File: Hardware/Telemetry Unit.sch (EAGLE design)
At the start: 12 parts, among them IC1 MEGA128-A, Q1 10MHz, U1 MPL3115A2, X1 SMA-142-0701-801/806

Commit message: First Pass at Compact Layout
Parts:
- removed X1: SMA-142-0701-801/806, con-coax:SMA-142-0701-801/806
- added B1: 9V_CLIP, TrackerPeripherals:9V_CLIP
- added C10, C9: 22u, resistor:C-USC0805
- added C11, C7, C8: 22p, resistor:C-USC0603
- added C5, C6: 2.2u, resistor:C-USC0603
- added D1: (no value), diode:DIODE-DO214AC
- added FIX, PWR: (no value), led:LEDSML0603
- added L1: 1.8n, TrackerPeripherals:L_SMALLL0603
- added L2: 6.8u, TrackerPeripherals:L_SMALLL1210
- added R1, R6: 10k, resistor:R-US_R0603
- added R10: 100k, resistor:R-US_R0603
- added R11, R2: 470, resistor:R-US_R0603
- added R3: 30k, resistor:R-US_R0603
- added R7: 40.2k, resistor:R-US_R0603
- added R8: 59k, resistor:R-US_R0603
- added R9: 13k, resistor:R-US_R0603
- added S1: TACT_SW_4.5MM, TrackerPeripherals:TACT_SW_4.5MM
- added U2: AP65111A, TrackerPeripherals:AP65111A
- C1: value (none) -> 2.2u
- GPS1: value TESO-LIV3F -> M20048-1; device ITCPeripherals:TESO-LIV3F -> TrackerPeripherals:M20048-1
- Q1: device crystal:CRYSTALCTS406 -> crystal:CRYSTALHC49UP
- U1: device ITCPeripherals:MPL3115A2 -> TrackerPeripherals:MPL3115A2
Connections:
- net N$4 renamed XTAL2
- net N$5 renamed XTAL1
- new net !GPS_SLP: GPS1.HW_S, IC1.(XCK1)PD5
- new net !RST: IC1.RESET, R1.2, S1.1@A, XB1.COORD_SEL/AD3/DIO3
- new net FIX: GPS1.FIX, IC1.(IC1)PD4, R2.1
- new net N$10: R8.1, U2.FB
- new net N$12: C11.1, U2.BST
- new net N$14: PWR.A, R11.2
- new net N$3: C7.2, GPS1.ANT_IN
- new net N$4: GPS1.AT2, L1.1
- new net N$5: IC1.PF0(ADC0), R3.2, R6.1
- new net N$6: FIX.A, R2.2
- new net N$7: C11.2, L2.1, U2.SW
- new net N$8: R7.2, R8.2, R9.1
- new net N$9: R10.2, U2.EN
- new net PROG_PWR: D1.A, XB1.RF_TX/AD4/DIO4
- new net RF_SLP: IC1.(T1)PD6, XB1.!DTR!/SLEEP_RQ/DI8
- new net VBAT: B1.+, C10.1, D1.C, R10.1, R3.1, U2.VIN
- net +3V3: now also C5.1, C6.1, C8.1, C9.1, GPS1.BV, L2.2, R1.1, R11.1, R7.1; no longer GPS1.VBAT, GPS1.VCC_IO, GPS1.VCC_RF
- net GND: now also B1.-, C10.2, C5.2, C6.2, C8.2, C9.2, FIX.C, GPS1.GND@1, GPS1.GND@10, GPS1.GND@11, GPS1.GND@12, GPS1.GND@13, GPS1.GND@14, GPS1.GND@2, GPS1.GND@3, GPS1.GND@4, GPS1.GND@5, GPS1.GND@6, GPS1.GND@7, GPS1.GND@8, GPS1.GND@9, L1.2, PWR.C, R6.2, R9.2, S1.0@B, U2.GND; no longer GPS1.GND, GPS1.GND_RF@1, GPS1.GND_RF@2, X1.2
- net N$1: now also C7.1, GPS1.ANT_OUT; no longer GPS1.RF_IN, X1.1
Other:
- note added: "0.25 attenuation with 2.56V ADC reference = 1mV per bit battery monitoring up to 10.24V"
- note added: "E2/E3 NC sets 9600 baud rate"

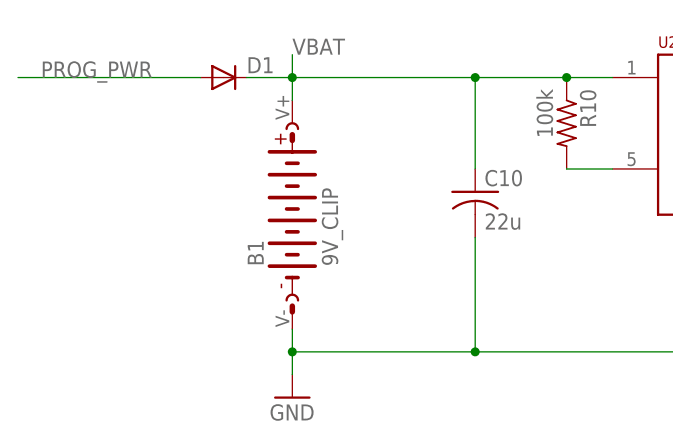
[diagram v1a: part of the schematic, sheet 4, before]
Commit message: Switch to screw terminals for battery
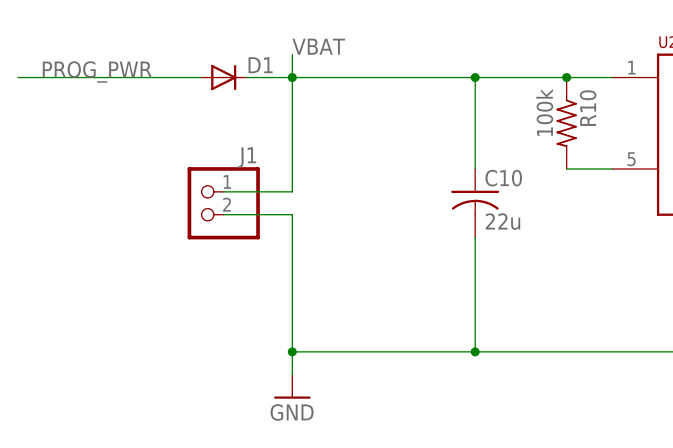
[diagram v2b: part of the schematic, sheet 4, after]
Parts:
- removed B1: 9V_CLIP, TrackerPeripherals:9V_CLIP
- added J1: (no value), TrackerPeripherals:ST_2X1
- C3, C4: value (none) -> 22p
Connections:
- new net N$11: IC1.RESET, S1.1@A
- net !RST: now also S1.1@B; no longer IC1.RESET, S1.1@A
- net GND: now also J1.2; no longer B1.-
- net VBAT: now also J1.1; no longer B1.+

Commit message: Add accelerometer
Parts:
- added C12: 100n, resistor:C-USC0603
- added C13: 2.2u, resistor:C-USC0603
- added U3: LSM6DS3, TrackerPeripherals:LSM6DS3
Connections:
- new net ACCEL_INT: IC1.(OC3B/INT4)PE4, U3.INT1
- net +3V3: now also C12.1, C13.1, U3.VDD, U3.VDDIO
- net GND: now also C12.2, C13.2, U3.GND@1, U3.GND@2
- net SCL: now also U3.SCL
- net SDA: now also U3.SDA

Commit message: Preliminary Signal Routing
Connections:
- removed net N$11: IC1.RESET, S1.1@A
- new net RST2: R1.2, S1.1@B
- net !RST: now also IC1.RESET, S1.1@A; no longer R1.2, S1.1@B
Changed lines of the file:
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@@
-</segment>
-</net>
-<net name="!RST" class="0">
-<segment>
-<label x="15.24" y="116.84" size="1.778" layer="95"/>
-<pinref part="S1" gate="G$1" pin="1@B"/>
-<pinref part="R1" gate="G$1" pin="2"/>
-<wire x1="22.86" y1="119.38" x2="22.86" y2="116.84" width="0.1524" layer="91"/>
-<wire x1="22.86" y1="116.84" x2="15.24" y2="114.3" width="0.1524" layer="91"/>
 </segment>
 </net>
@@
 </segment>
 </net>
-<net name="N$11" class="0">
+<net name="!RST" class="0">
 <segment>
 <pinref part="IC1" gate="G$1" pin="RESET"/>
@@
 <wire x1="15.24" y1="116.84" x2="22.86" y2="114.3" width="0.1524" layer="91"/>
 <wire x1="22.86" y1="114.3" x2="25.4" y2="114.3" width="0.1524" layer="91"/>
+<label x="15.24" y="116.84" size="1.778" layer="95"/>
 </segment>
 </net>
@@
 </segment>
 </net>
+<net name="RST2" class="0">
+<segment>
+<pinref part="S1" gate="G$1" pin="1@B"/>
+<pinref part="R1" gate="G$1" pin="2"/>
+<wire x1="22.86" y1="119.38" x2="22.86" y2="116.84" width="0.1524" layer="91"/>
+<wire x1="22.86" y1="116.84" x2="15.24" y2="114.3" width="0.1524" layer="91"/>
+</segment>
+</net>

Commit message: Merging changes into schematics.
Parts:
- added C14: 100nF, rcl:C-EUC0603
- added IC2: FT232RL, ftdichip:FT232RL
- added J2: 503182-1852, 503182-1852_SD:503182-1852
- added J3: 10118193-0001LF, 10118193-0001LF_microUSB:10118193-0001LF
- added LED1, LED2: (no value), led:LEDCHIP-LED0603
- added R12, R13: 1k, rcl:R-US_R0603
- added R14: 10k, rcl:R-US_R0603
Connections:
- new net CS_SD: IC1.(OC0)PB4, J2.DATA2, R14.1
- new net N$11: IC2.USBDM, J3.D-
- new net N$13: IC2.USBDP, J3.D+
- new net N$15: LED1.C, R12.1
- new net N$16: C14.1, IC2.!DTR
- new net N$17: LED2.C, R13.1
- new net N$18: IC2.CBUS1, R12.2
- new net N$19: IC2.CBUS0, R13.2
- new net V_USB: J3.VUSB
- net !RST: now also C14.2
- net +3V3: now also J2.VDD, R14.2
- net GND: now also IC2.!RESET, IC2.GND, IC2.GND@1, IC2.GND@2, IC2.GND@A, IC2.TEST, J2.SHIELD, J2.VSS, J3.GND, J3.SHIELD
- net MISO: now also J2.DAT0
- net MOSI: now also J2.CMD
- net RX0: now also IC2.TXD
- net SCK: now also J2.CLK
- net TX0: now also IC2.RXD
- net VCC: now also IC2.VCC, IC2.VCCIO, LED1.A, LED2.A

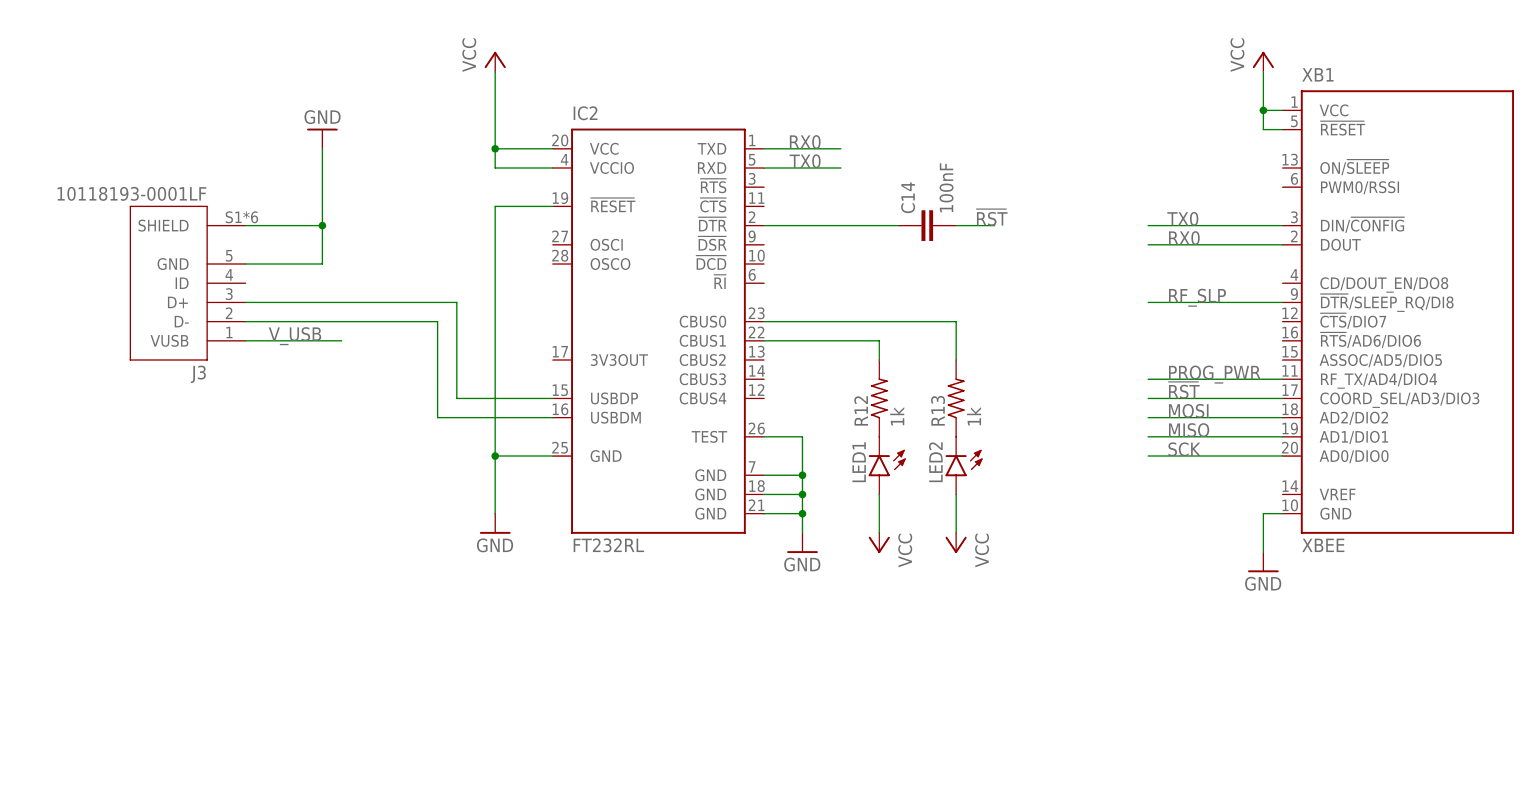
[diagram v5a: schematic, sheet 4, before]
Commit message: Finished merge, updated layout, added ICSP
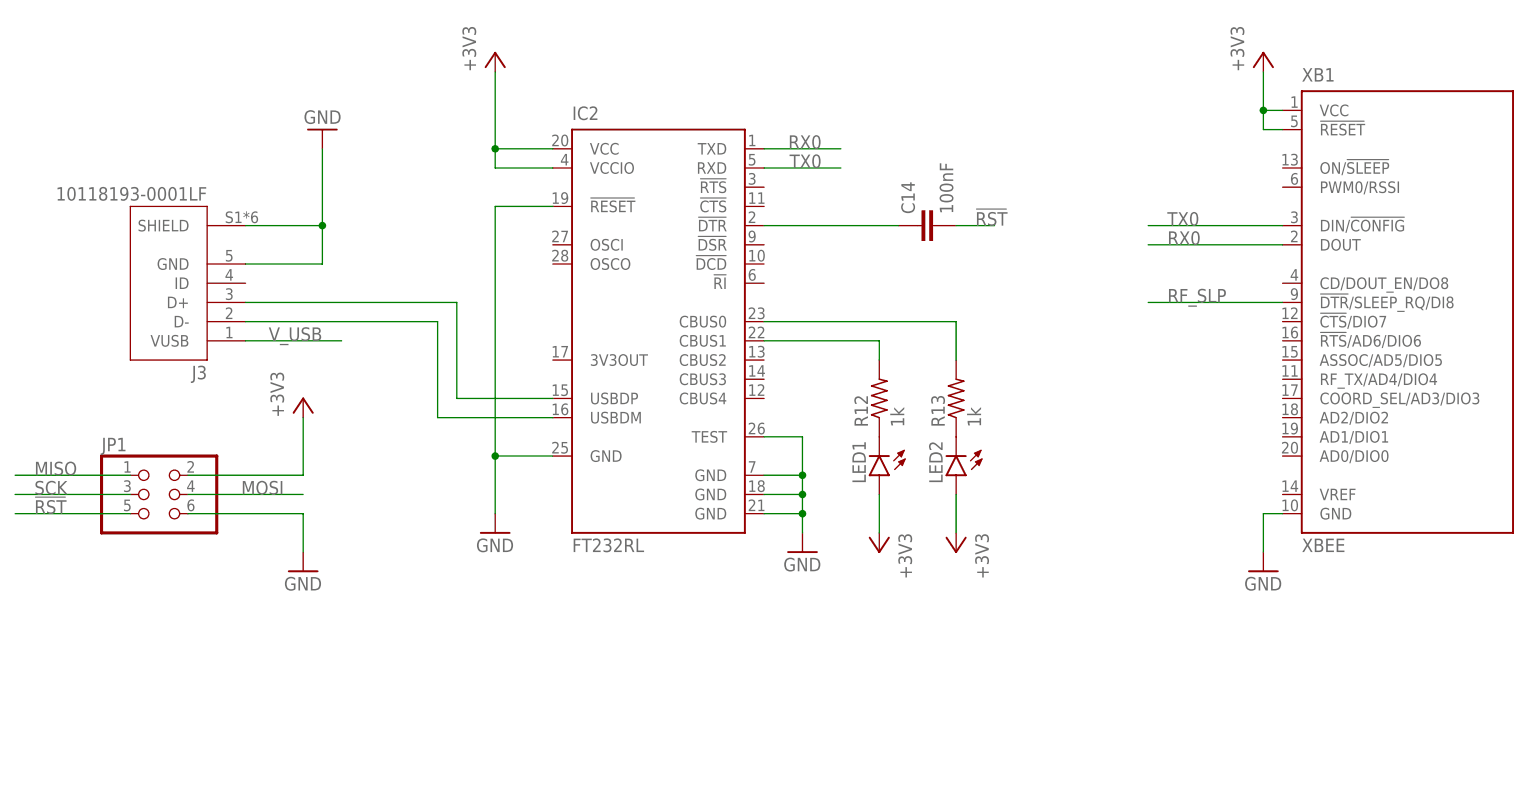
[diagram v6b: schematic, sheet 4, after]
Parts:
- added JP1: (no value), pinhead:PINHD-2X3
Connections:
- removed net PROG_PWR: D1.A, XB1.RF_TX/AD4/DIO4
- removed net VCC: IC2.VCC, IC2.VCCIO, LED1.A, LED2.A, XB1.!RESET, XB1.VCC
- net !RST: now also JP1.5; no longer XB1.COORD_SEL/AD3/DIO3
- net +3V3: now also IC2.VCC, IC2.VCCIO, JP1.2, LED1.A, LED2.A, XB1.!RESET, XB1.VCC
- net GND: now also JP1.6
- net MISO: now also JP1.1; no longer XB1.AD1/DIO1
- net MOSI: now also JP1.4; no longer XB1.AD2/DIO2
- net SCK: now also JP1.3; no longer XB1.AD0/DIO0
- net V_USB: now also D1.A

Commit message: Full Routing Complete?
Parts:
- added C15: 2.2u, resistor:C-USC0603
- added R15, R16: 10k, resistor:R-US_R0603
- renumbered LED1 to RX, LED2 to TX
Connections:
- new net N$20: IC2.TXD, R15.1
- new net N$21: IC2.RXD, R16.1
- net !RST: no longer C14.2, JP1.5
- net +3V3: now also C15.1
- net GND: now also C15.2, GPS1.AT1, S1.0@A
- net RST2: now also C14.2, JP1.5
- net RX0: now also R15.2; no longer IC2.TXD
- net TX0: now also R16.2; no longer IC2.RXD
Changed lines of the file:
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@@
 <part name="R12" library="rcl" library_urn="urn:adsk.eagle:library:334" deviceset="R-US_" device="R0603" package3d_urn="urn:adsk.eagle:package:23555/2" value="1k"/>
 <part name="R13" library="rcl" library_urn="urn:adsk.eagle:library:334" deviceset="R-US_" device="R0603" package3d_urn="urn:adsk.eagle:package:23555/2" value="1k"/>
-<part name="LED1" library="led" library_urn="urn:adsk.eagle:library:259" deviceset="LED" device="CHIP-LED0603" package3d_urn="urn:adsk.eagle:package:15819/3"/>
-<part name="LED2" library="led" library_urn="urn:adsk.eagle:library:259" deviceset="LED" device="CHIP-LED0603" package3d_urn="urn:adsk.eagle:package:15819/3"/>
+<part name="RX" library="led" library_urn="urn:adsk.eagle:library:259" deviceset="LED" device="CHIP-LED0603" package3d_urn="urn:adsk.eagle:package:15819/3"/>
+<part name="TX" library="led" library_urn="urn:adsk.eagle:library:259" deviceset="LED" device="CHIP-LED0603" package3d_urn="urn:adsk.eagle:package:15819/3"/>
 <part name="P+3" library="supply1" library_urn="urn:adsk.eagle:library:371" deviceset="+3V3" device=""/>
 <part name="P+4" library="supply1" library_urn="urn:adsk.eagle:library:371" deviceset="+3V3" device=""/>
@@
 <part name="GND19" library="supply1" library_urn="urn:adsk.eagle:library:371" deviceset="GND" device=""/>
 <part name="P+5" library="supply1" library_urn="urn:adsk.eagle:library:371" deviceset="+3V3" device=""/>
+<part name="C15" library="resistor" library_urn="urn:adsk.eagle:library:348" deviceset="C-US" device="C0603" package3d_urn="urn:adsk.eagle:package:23616/2" value="2.2u"/>
+<part name="R15" library="resistor" library_urn="urn:adsk.eagle:library:348" deviceset="R-US_" device="R0603" package3d_urn="urn:adsk.eagle:package:23555/3" value="10k"/>
+<part name="R16" library="resistor" library_urn="urn:adsk.eagle:library:348" deviceset="R-US_" device="R0603" package3d_urn="urn:adsk.eagle:package:23555/3" value="10k"/>
 </parts>
 <sheets>
@@
 <pinref part="GND7" gate="1" pin="GND"/>
 <pinref part="S1" gate="G$1" pin="0@B"/>
+<pinref part="S1" gate="G$1" pin="0@A"/>
+<wire x1="2.54" y1="116.84" x2="-2.54" y2="116.84" width="0.1524" layer="91"/>
+<wire x1="-2.54" y1="116.84" x2="-2.54" y2="114.3" width="0.1524" layer="91"/>
+<junction x="-2.54" y="114.3"/>
 </segment>
 <segment>
@@
 <pinref part="GND1" gate="1" pin="GND"/>
 <wire x1="73.66" y1="50.8" x2="73.66" y2="48.26" width="0.1524" layer="91"/>
+<pinref part="GPS1" gate="G$1" pin="AT1"/>
+<wire x1="45.72" y1="53.34" x2="45.72" y2="55.88" width="0.1524" layer="91"/>
+<wire x1="45.72" y1="55.88" x2="73.66" y2="55.88" width="0.1524" layer="91"/>
+<wire x1="73.66" y1="55.88" x2="73.66" y2="50.8" width="0.1524" layer="91"/>
+<junction x="73.66" y="50.8"/>
 </segment>
 <segment>
@@
 </instance>
 <instance part="C14" gate="G$1" x="25.4" y="66.04" smashed="yes" rot="R90">
-<attribute name="NAME" x="25.019" y="67.564" size="1.778" layer="95" rot="R90"/>
-<attribute name="VALUE" x="30.099" y="67.564" size="1.778" layer="96" rot="R90"/>
+<attribute name="NAME" x="23.876" y="65.659" size="1.778" layer="95" rot="R180"/>
+<attribute name="VALUE" x="26.416" y="63.119" size="1.778" layer="96" rot="R180"/>
 </instance>
 <instance part="R12" gate="G$1" x="20.32" y="43.18" smashed="yes" rot="R90">
@@
 <attribute name="VALUE" x="33.782" y="39.37" size="1.778" layer="96" rot="R90"/>
 </instance>
-<instance part="LED1" gate="G$1" x="20.32" y="33.02" smashed="yes" rot="R180">
+<instance part="RX" gate="G$1" x="20.32" y="33.02" smashed="yes" rot="R180">
 <attribute name="NAME" x="16.764" y="37.592" size="1.778" layer="95" rot="R270"/>
 <attribute name="VALUE" x="14.605" y="37.592" size="1.778" layer="96" rot="R270"/>
 </instance>
-<instance part="LED2" gate="G$1" x="30.48" y="33.02" smashed="yes" rot="R180">
+<instance part="TX" gate="G$1" x="30.48" y="33.02" smashed="yes" rot="R180">
 <attribute name="NAME" x="26.924" y="37.592" size="1.778" layer="95" rot="R270"/>
 <attribute name="VALUE" x="24.765" y="37.592" size="1.778" layer="96" rot="R270"/>
@@
 <instance part="P+5" gate="G$1" x="-55.88" y="43.18" smashed="yes">
 <attribute name="VALUE" x="-58.42" y="40.64" size="1.778" layer="96" rot="R90"/>
+</instance>
+<instance part="C15" gate="G$1" x="-35.56" y="71.12" smashed="yes">
+<attribute name="NAME" x="-34.544" y="71.755" size="1.778" layer="95"/>
+<attribute name="VALUE" x="-34.544" y="66.929" size="1.778" layer="96"/>
+</instance>
+<instance part="R15" gate="G$1" x="20.32" y="76.2" smashed="yes">
+<attribute name="NAME" x="16.51" y="77.6986" size="1.778" layer="95"/>
+<attribute name="VALUE" x="21.59" y="77.978" size="1.778" layer="96"/>
+</instance>
+<instance part="R16" gate="G$1" x="20.32" y="73.66" smashed="yes">
+<attribute name="NAME" x="16.51" y="70.0786" size="1.778" layer="95"/>
+<attribute name="VALUE" x="21.59" y="70.358" size="1.778" layer="96"/>
 </instance>
 </instances>
@@
 <pinref part="IC2" gate="1" pin="!RESET"/>
 <wire x1="-22.86" y1="68.58" x2="-30.48" y2="68.58" width="0.1524" layer="91"/>
-<wire x1="-30.48" y1="68.58" x2="-30.48" y2="35.56" width="0.1524" layer="91"/>
+<wire x1="-30.48" y1="68.58" x2="-30.48" y2="66.04" width="0.1524" layer="91"/>
 <pinref part="GND17" gate="1" pin="GND"/>
 <pinref part="IC2" gate="1" pin="GND@A"/>
+<wire x1="-30.48" y1="66.04" x2="-30.48" y2="35.56" width="0.1524" layer="91"/>
 <wire x1="-30.48" y1="35.56" x2="-30.48" y2="27.94" width="0.1524" layer="91"/>
 <wire x1="-22.86" y1="35.56" x2="-30.48" y2="35.56" width="0.1524" layer="91"/>
 <junction x="-30.48" y="35.56"/>
+<pinref part="C15" gate="G$1" pin="2"/>
+<wire x1="-35.56" y1="66.04" x2="-30.48" y2="66.04" width="0.1524" layer="91"/>
+<junction x="-30.48" y="66.04"/>
 </segment>
 <segment>
@@
 </segment>
 <segment>
-<pinref part="IC2" gate="1" pin="RXD"/>
-<wire x1="5.08" y1="73.66" x2="15.24" y2="73.66" width="0.1524" layer="91"/>
-<label x="12.7" y="73.66" size="1.778" layer="95" align="bottom-right"/>
+<pinref part="R16" gate="G$1" pin="2"/>
+<wire x1="25.4" y1="73.66" x2="35.56" y2="73.66" width="0.1524" layer="91"/>
+<label x="33.02" y="73.66" size="1.778" layer="95" align="bottom-right"/>
 </segment>
 </net>
@@
 </segment>
 <segment>
-<pinref part="IC2" gate="1" pin="TXD"/>
-<wire x1="5.08" y1="76.2" x2="15.24" y2="76.2" width="0.1524" layer="91"/>
-<label x="12.7" y="76.2" size="1.778" layer="95" align="bottom-right"/>
-</segment>
-</net>
-<net name="!RST" class="0">
-<segment>
-<pinref part="C14" gate="G$1" pin="2"/>
-<wire x1="30.48" y1="66.04" x2="35.56" y2="66.04" width="0.1524" layer="91"/>
-<label x="33.02" y="66.04" size="1.778" layer="95"/>
-</segment>
-<segment>
-<pinref part="JP1" gate="A" pin="5"/>
-<wire x1="-78.74" y1="27.94" x2="-93.98" y2="27.94" width="0.1524" layer="91"/>
-<label x="-91.44" y="27.94" size="1.778" layer="95"/>
+<pinref part="R15" gate="G$1" pin="2"/>
+<wire x1="25.4" y1="76.2" x2="35.56" y2="76.2" width="0.1524" layer="91"/>
+<label x="33.02" y="76.2" size="1.778" layer="95" align="bottom-right"/>
 </segment>
 </net>
@@
 <segment>
 <pinref part="R12" gate="G$1" pin="1"/>
-<pinref part="LED1" gate="G$1" pin="C"/>
+<pinref part="RX" gate="G$1" pin="C"/>
 </segment>
 </net>
@@
 <segment>
 <pinref part="R13" gate="G$1" pin="1"/>
-<pinref part="LED2" gate="G$1" pin="C"/>
+<pinref part="TX" gate="G$1" pin="C"/>
 </segment>
 </net>
@@
 <wire x1="-30.48" y1="73.66" x2="-30.48" y2="76.2" width="0.1524" layer="91"/>
 <junction x="-30.48" y="76.2"/>
+<pinref part="C15" gate="G$1" pin="1"/>
+<wire x1="-35.56" y1="73.66" x2="-30.48" y2="73.66" width="0.1524" layer="91"/>
+<junction x="-30.48" y="73.66"/>
 </segment>
 <segment>
 <pinref part="P+3" gate="G$1" pin="+3V3"/>
-<pinref part="LED1" gate="G$1" pin="A"/>
+<pinref part="RX" gate="G$1" pin="A"/>
 <wire x1="20.32" y1="25.4" x2="20.32" y2="30.48" width="0.1524" layer="91"/>
 </segment>
 <segment>
 <pinref part="P+4" gate="G$1" pin="+3V3"/>
-<pinref part="LED2" gate="G$1" pin="A"/>
+<pinref part="TX" gate="G$1" pin="A"/>
 <wire x1="30.48" y1="25.4" x2="30.48" y2="30.48" width="0.1524" layer="91"/>
 </segment>
@@
 </segment>
 </net>
+<net name="RST2" class="0">
+<segment>
+<pinref part="C14" gate="G$1" pin="2"/>
+<wire x1="30.48" y1="66.04" x2="35.56" y2="66.04" width="0.1524" layer="91"/>
+<label x="33.02" y="66.04" size="1.778" layer="95"/>
+</segment>
+<segment>
+<pinref part="JP1" gate="A" pin="5"/>
+<wire x1="-78.74" y1="27.94" x2="-93.98" y2="27.94" width="0.1524" layer="91"/>
+<label x="-91.44" y="27.94" size="1.778" layer="95"/>
+</segment>
+</net>
+<net name="N$20" class="0">
+<segment>
+<pinref part="R15" gate="G$1" pin="1"/>
+<pinref part="IC2" gate="1" pin="TXD"/>
+<wire x1="15.24" y1="76.2" x2="5.08" y2="76.2" width="0.1524" layer="91"/>
+</segment>
+</net>
+<net name="N$21" class="0">
+<segment>
+<pinref part="IC2" gate="1" pin="RXD"/>
+<pinref part="R16" gate="G$1" pin="1"/>
+<wire x1="5.08" y1="73.66" x2="15.24" y2="73.66" width="0.1524" layer="91"/>
+</segment>
+</net>

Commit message: Fix USB port nonsense/xBee logo
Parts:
- XB1: device maxstream:XBEE -> TrackerPeripherals:XBEE
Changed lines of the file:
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@@
 <part name="C4" library="resistor" library_urn="urn:adsk.eagle:library:348" deviceset="C-US" device="C0603" package3d_urn="urn:adsk.eagle:package:23616/2" value="22p"/>
 <part name="GND4" library="supply1" library_urn="urn:adsk.eagle:library:371" deviceset="GND" device=""/>
-<part name="XB1" library="maxstream" library_urn="urn:adsk.eagle:library:270" deviceset="XBEE" device="" package3d_urn="urn:adsk.eagle:package:18007/1"/>
+<part name="XB1" library="TrackerPeripherals" deviceset="XBEE" device="" package3d_urn="urn:adsk.eagle:package:18007/1"/>
 <part name="P+1" library="supply1" library_urn="urn:adsk.eagle:library:371" deviceset="+3V3" device=""/>
 <part name="GND5" library="supply1" library_urn="urn:adsk.eagle:library:371" deviceset="GND" device=""/>
